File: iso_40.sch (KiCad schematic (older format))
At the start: 14 parts

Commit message: layout png
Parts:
- added F?: 500mA, symbol Device:Polyfuse_Small
- added USB?: Molex-0548190589, symbol random-keyboard-parts:Molex-0548190589
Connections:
- net +5V: now also F?.1
- net D+: now also USB?.3 (D+)
- net D-: now also USB?.4 (D-)
- net GND: now also USB?.1 (GND)
- new net VCC: F?.2, USB?.5 (VBUS)
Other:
- moved on the sheet: C?, R?, SW?, U?, Y?

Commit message: pcb routed
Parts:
- added D1, D10, D11, D12, D13, D14, D15, D16, D17, D18, D19, D2, D20, D21, D22, D23, D24, D25, D26, D27, D28, D29, D3, D30, D31, D32, D33, D34, D35, D36, D37, D38, D39, D4, D40, D5, D6, D7, D8, D9: SOD-123, Diode_SMD:D_SOD-123, symbol Device:D_Small
- added MX1, MX10, MX11, MX14, MX15, MX16, MX17, MX18, MX19, MX2, MX20, MX21, MX22, MX23, MX25, MX26, MX27, MX28, MX29, MX3, MX30, MX31, MX32, MX33, MX34, MX35, MX36, MX4, MX40, MX5, MX6, MX7, MX8, MX9: MX-NoLED, MX_Only:MXOnly-1U-NoLED, symbol MX_Alps_Hybrid:MX-NoLED
- added MX12: MX-NoLED, MX_Only:MXOnly-ISO, symbol MX_Alps_Hybrid:MX-NoLED
- added MX13: MX-NoLED, MX_Only:MXOnly-1.25U-NoLED, symbol MX_Alps_Hybrid:MX-NoLED
- added MX24, MX37, MX39: MX-NoLED, MX_Only:MXOnly-1.5U-NoLED, symbol MX_Alps_Hybrid:MX-NoLED
- added MX38: MX-NoLED, MX_Only:MXOnly-6U-NoLED, symbol MX_Alps_Hybrid:MX-NoLED
- C1, C2, C3, C4, C5, C6, C7: renamed from C?; footprint (none) -> Capacitor_SMD:C_0805_2012Metric
- F1: renamed from F?; footprint (none) -> Fuse:Fuse_1206_3216Metric
- R1, R2, R3, R4: renamed from R?; footprint (none) -> Resistor_SMD:R_0805_2012Metric
- SW1: renamed from SW?; footprint (none) -> random-keyboard-parts:SKQG-1155865
- USB1: renamed from USB?; footprint (none) -> random-keyboard-parts:Molex-0548190589
- Y1: renamed from Y?; footprint (none) -> Crystal:Crystal_SMD_3225-4Pin_3.2x2.5mm
- gave numbers to parts that had none: 1
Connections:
- net col_08: now reaches U1.10 (PB2)
- net col_08: now also MX21.1 (COL), MX32.1 (COL), MX9.1 (COL)
- net col_09: now reaches U1.11 (PB3)
- net col_09: now also MX10.1 (COL), MX22.1 (COL), MX33.1 (COL), MX39.1 (COL)
- net col_06: now reaches U1.12 (PB7)
- net col_06: now also MX19.1 (COL), MX30.1 (COL), MX38.1 (COL), MX7.1 (COL)
- net col_10: now reaches U1.18 (PD0)
- net col_10: now also MX11.1 (COL), MX23.1 (COL), MX34.1 (COL), MX40.1 (COL)
- net col_11: now reaches U1.19 (PD1)
- net col_11: now also MX12.1 (COL), MX35.1 (COL)
- net row_2: now reaches U1.20 (PD2)
- net row_2: now also D24.1 (K), D25.1 (K), D26.1 (K), D27.1 (K), D28.1 (K), D29.1 (K), D30.1 (K), D31.1 (K), D32.1 (K), D33.1 (K), D34.1 (K), D35.1 (K)
- net row_1: now reaches U1.21 (PD3)
- net row_1: now also D13.1 (K), D14.1 (K), D15.1 (K), D16.1 (K), D17.1 (K), D18.1 (K), D19.1 (K), D20.1 (K), D21.1 (K), D22.1 (K), D23.1 (K)
- net row_0: now reaches U1.22 (PD5)
- net row_0: now also D1.1 (K), D10.1 (K), D11.1 (K), D12.1 (K), D2.1 (K), D3.1 (K), D4.1 (K), D5.1 (K), D6.1 (K), D7.1 (K), D8.1 (K), D9.1 (K)
- net row_3: now reaches U1.25 (PD4)
- net row_3: now also D36.1 (K), D37.1 (K), D38.1 (K), D39.1 (K), D40.1 (K)
- net col_04: now reaches U1.37 (PF6)
- net col_04: now also MX17.1 (COL), MX28.1 (COL), MX5.1 (COL)
- net col_03: now reaches U1.38 (PF5)
- net col_03: now also MX16.1 (COL), MX27.1 (COL), MX4.1 (COL)
- net col_02: now reaches U1.39 (PF4)
- net col_02: now also MX15.1 (COL), MX26.1 (COL), MX3.1 (COL)
- net col_01: now reaches U1.40 (PF1)
- net col_01: now also MX14.1 (COL), MX2.1 (COL), MX25.1 (COL), MX37.1 (COL)
- net col_00: now reaches U1.41 (PF0)
- net col_00: now also MX1.1 (COL), MX13.1 (COL), MX24.1 (COL), MX36.1 (COL)
- net col_05: now reaches U1.8 (PB0)
- net col_05: now also MX18.1 (COL), MX29.1 (COL), MX6.1 (COL)
- net col_07: now reaches U1.9 (PB1)
- net col_07: now also MX20.1 (COL), MX31.1 (COL), MX8.1 (COL)
- new net: D1.2 (A), MX1.2 (ROW)
- new net: D2.2 (A), MX2.2 (ROW)
- new net: D3.2 (A), MX3.2 (ROW)
- new net: D4.2 (A), MX4.2 (ROW)
- new net: D5.2 (A), MX5.2 (ROW)
- new net: D6.2 (A), MX6.2 (ROW)
- new net: D7.2 (A), MX7.2 (ROW)
- new net: D8.2 (A), MX8.2 (ROW)
- new net: D9.2 (A), MX9.2 (ROW)
- new net: D10.2 (A), MX10.2 (ROW)
- new net: D11.2 (A), MX11.2 (ROW)
- new net: D12.2 (A), MX12.2 (ROW)
- new net: D13.2 (A), MX13.2 (ROW)
- new net: D14.2 (A), MX14.2 (ROW)
- new net: D15.2 (A), MX15.2 (ROW)
- new net: D16.2 (A), MX16.2 (ROW)
- new net: D17.2 (A), MX17.2 (ROW)
- new net: D18.2 (A), MX18.2 (ROW)
- new net: D19.2 (A), MX19.2 (ROW)
- new net: D20.2 (A), MX20.2 (ROW)
- new net: D21.2 (A), MX21.2 (ROW)
- new net: D22.2 (A), MX22.2 (ROW)
- new net: D23.2 (A), MX23.2 (ROW)
- new net: D24.2 (A), MX24.2 (ROW)
- new net: D25.2 (A), MX25.2 (ROW)
- new net: D26.2 (A), MX26.2 (ROW)
- new net: D27.2 (A), MX27.2 (ROW)
- new net: D28.2 (A), MX28.2 (ROW)
- new net: D29.2 (A), MX29.2 (ROW)
- new net: D30.2 (A), MX30.2 (ROW)
- new net: D31.2 (A), MX31.2 (ROW)
- new net: D32.2 (A), MX32.2 (ROW)
- new net: D33.2 (A), MX33.2 (ROW)
- new net: D34.2 (A), MX34.2 (ROW)
- new net: D35.2 (A), MX35.2 (ROW)
- new net: D37.2 (A), MX37.2 (ROW)
- new net: D36.2 (A), MX36.2 (ROW)
- new net: D38.2 (A), MX38.2 (ROW)
- new net: D40.2 (A), MX40.2 (ROW)
- new net: D39.2 (A), MX39.2 (ROW)
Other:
- moved on the sheet: F1, USB1

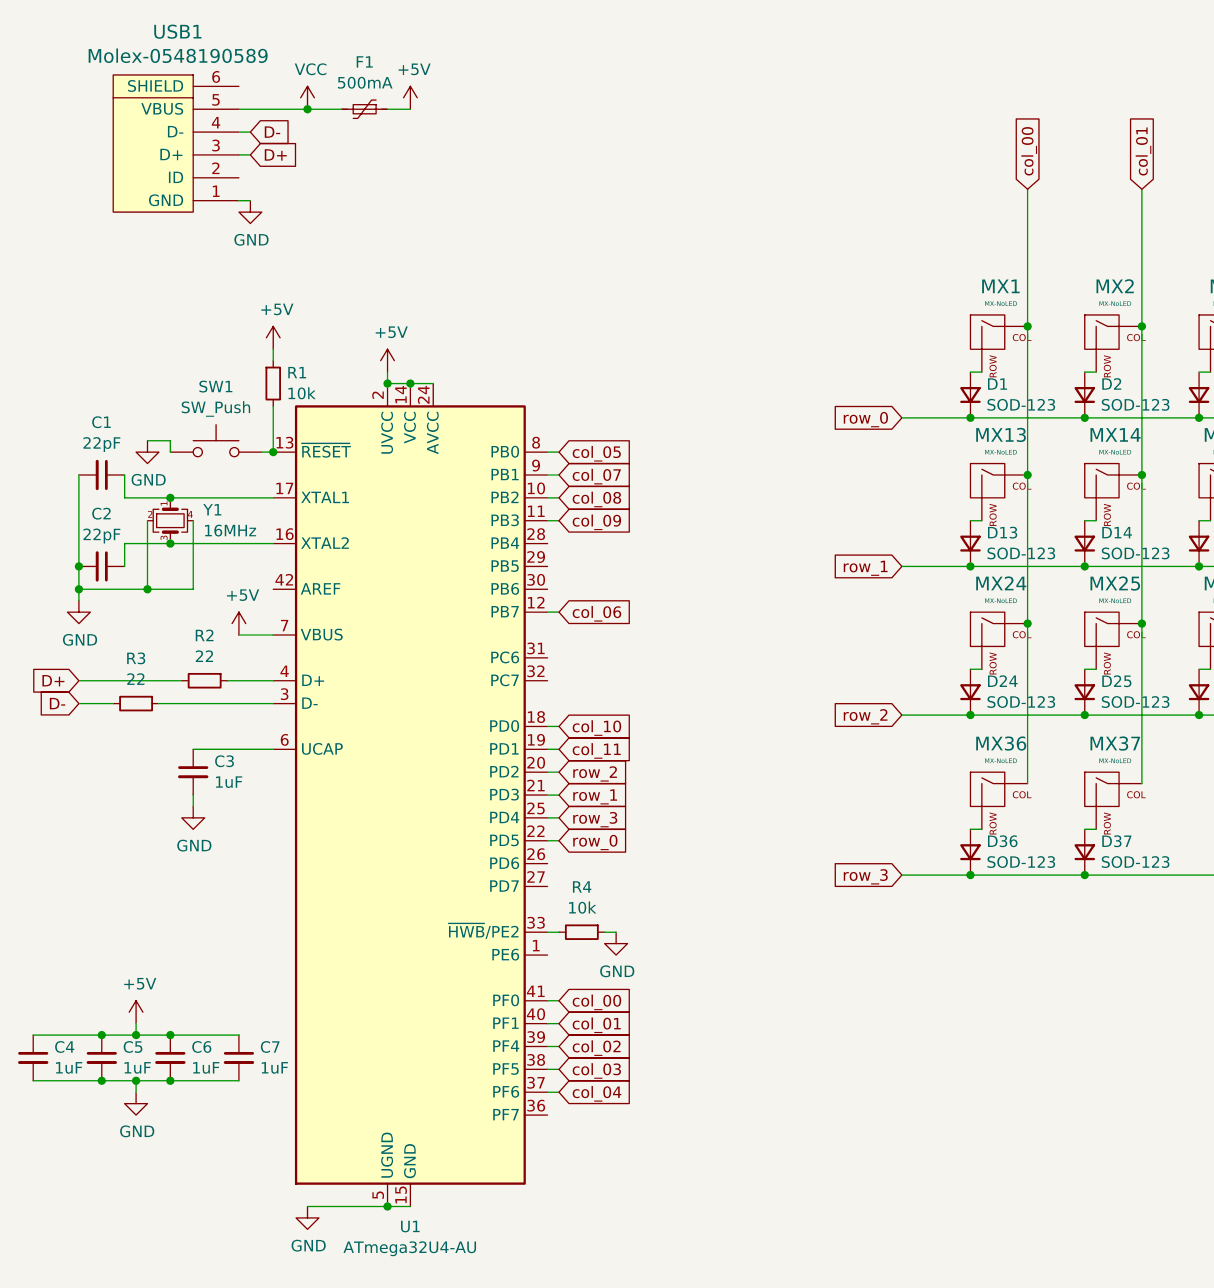
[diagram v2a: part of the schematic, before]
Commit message: ISP header added
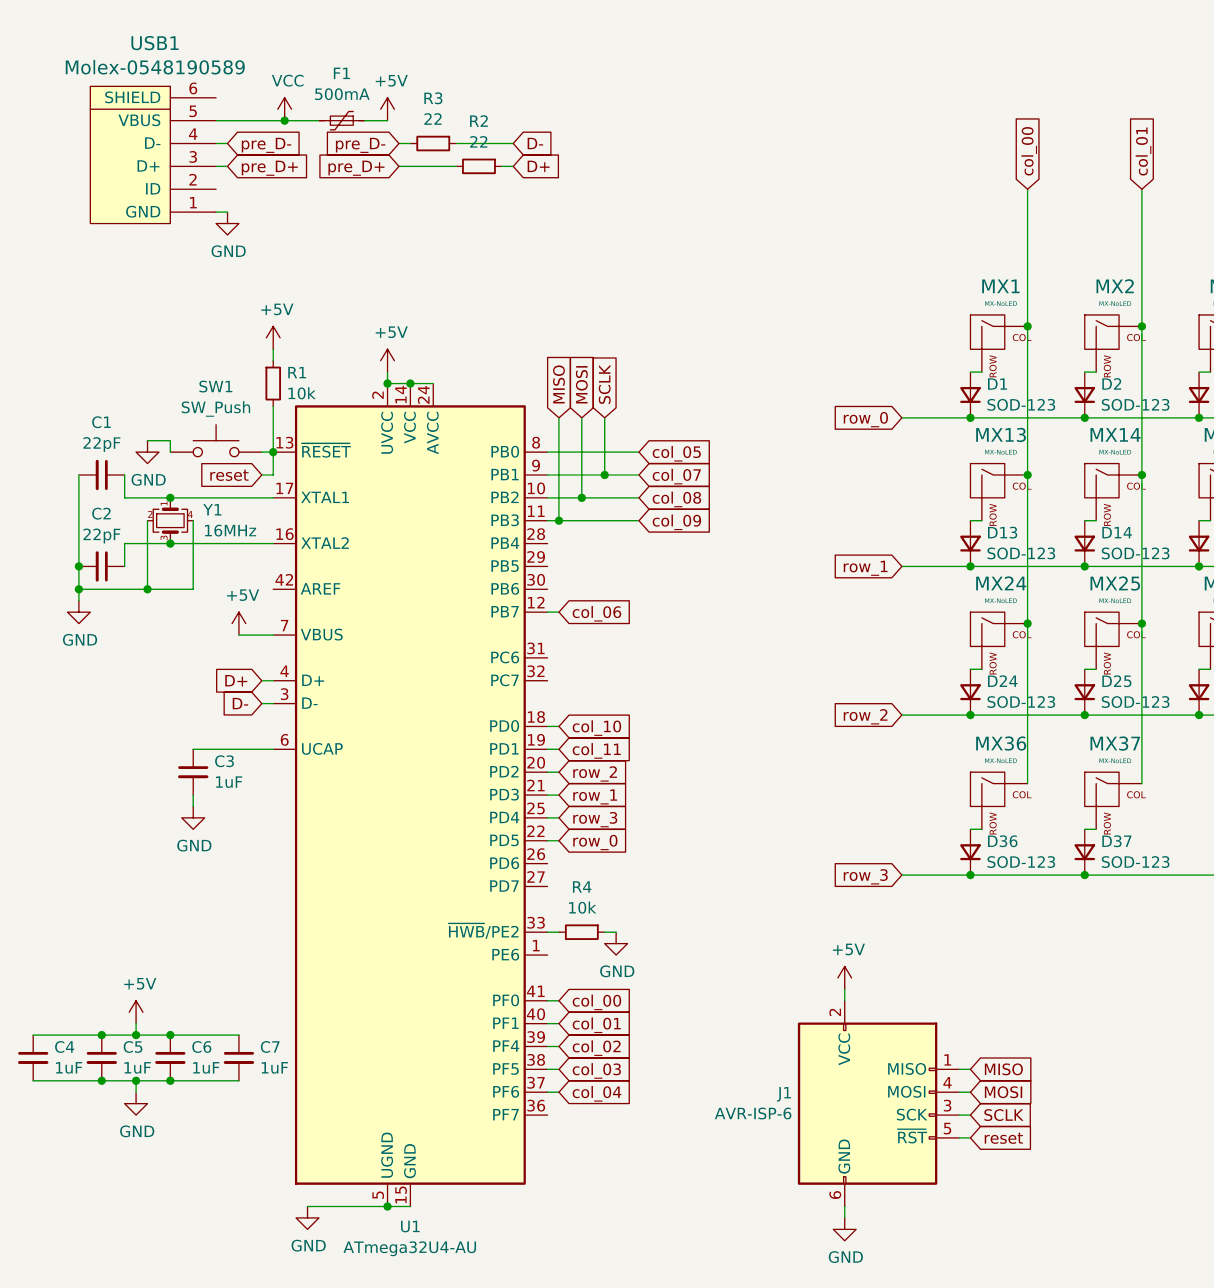
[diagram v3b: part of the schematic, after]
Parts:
- added J1: AVR-ISP-6, Connector_PinHeader_2.54mm:PinHeader_2x03_P2.54mm_Vertical, symbol Connector:AVR-ISP-6
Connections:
- net +5V: now also J1.2 (VCC)
- net D+: now also R2.1, U1.4 (D+); no longer R2.2, USB1.3 (D+)
- net D-: now also R3.1, U1.3 (D-); no longer R3.2, USB1.4 (D-)
- net GND: now also J1.6 (GND)
- net reset: now reaches R1.2, SW1.2, U1.13 (~RESET)
- net reset: now also J1.5 (~RST)
- net col_07 renamed SCLK
- net SCLK: now also J1.3 (SCK)
- net col_08 renamed MOSI
- net MOSI: now also J1.4 (MOSI)
- net col_09 renamed MISO
- net MISO: now also J1.1 (MISO)
- new net pre_D+: R2.2, USB1.3 (D+)
- new net pre_D-: R3.2, USB1.4 (D-)
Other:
- moved on the sheet: F1, R2, R3, USB1
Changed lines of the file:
@@
 L Device:R_Small R3
 U 1 1 5F1598E0
-P 1100 5250
-F 0 "R3" V 904 5250 50  0000 C CNN
-F 1 "22" V 995 5250 50  0000 C CNN
-F 2 "Resistor_SMD:R_0805_2012Metric" H 1100 5250 50  0001 C CNN
-F 3 "~" H 1100 5250 50  0001 C CNN
-	1    1100 5250
+P 2400 2800
+F 0 "R3" V 2204 2800 50  0000 C CNN
+F 1 "22" V 2295 2800 50  0000 C CNN
+F 2 "Resistor_SMD:R_0805_2012Metric" H 2400 2800 50  0001 C CNN
+F 3 "~" H 2400 2800 50  0001 C CNN
+	1    2400 2800
 	0    1    1    0
 $EndComp
@@
 L Device:R_Small R2
 U 1 1 5F1590A4
-P 1400 5150
-F 0 "R2" V 1204 5150 50  0000 C CNN
-F 1 "22" V 1295 5150 50  0000 C CNN
-F 2 "Resistor_SMD:R_0805_2012Metric" H 1400 5150 50  0001 C CNN
-F 3 "~" H 1400 5150 50  0001 C CNN
-	1    1400 5150
+P 2600 2900
+F 0 "R2" V 2404 2900 50  0000 C CNN
+F 1 "22" V 2495 2900 50  0000 C CNN
+F 2 "Resistor_SMD:R_0805_2012Metric" H 2600 2900 50  0001 C CNN
+F 3 "~" H 2600 2900 50  0001 C CNN
+	1    2600 2900
 	0    1    1    0
 $EndComp
-Wire Wire Line
-	1700 5150 1500 5150
-Wire Wire Line
-	1700 5250 1200 5250
 $Comp
 L Device:Crystal_GND24_Small Y1
@@
 Wire Wire Line
 	1700 3700 1700 3750
-Text GLabel 850  5150 0    50   Input ~ 0
+Text GLabel 1650 5150 0    50   Input ~ 0
 D+
-Text GLabel 850  5250 0    50   Input ~ 0
+Text GLabel 1650 5250 0    50   Input ~ 0
 D-
-Wire Wire Line
-	850  5150 1300 5150
-Wire Wire Line
-	850  5250 1000 5250
 $Comp
 L random-keyboard-parts:Molex-0548190589 USB1
 U 1 1 5F1AE520
-P 1250 2850
-F 0 "USB1" V 1787 2817 60  0000 C CNN
-F 1 "Molex-0548190589" V 1681 2817 60  0000 C CNN
-F 2 "random-keyboard-parts:Molex-0548190589" H 1250 2850 60  0001 C CNN
-F 3 "" H 1250 2850 60  0001 C CNN
-	1    1250 2850
+P 1150 2900
+F 0 "USB1" V 1687 2867 60  0000 C CNN
+F 1 "Molex-0548190589" V 1581 2867 60  0000 C CNN
+F 2 "random-keyboard-parts:Molex-0548190589" H 1150 2900 60  0001 C CNN
+F 3 "" H 1150 2900 60  0001 C CNN
+	1    1150 2900
 	0    -1   -1   0
 $EndComp
@@
 L Device:Polyfuse_Small F1
 U 1 1 5F1B31E3
-P 2100 2650
-F 0 "F1" V 1895 2650 50  0000 C CNN
-F 1 "500mA" V 1986 2650 50  0000 C CNN
-F 2 "Fuse:Fuse_1206_3216Metric" H 2150 2450 50  0001 L CNN
-F 3 "~" H 2100 2650 50  0001 C CNN
-	1    2100 2650
+P 2000 2700
+F 0 "F1" V 1795 2700 50  0000 C CNN
+F 1 "500mA" V 1886 2700 50  0000 C CNN
+F 2 "Fuse:Fuse_1206_3216Metric" H 2050 2500 50  0001 L CNN
+F 3 "~" H 2000 2700 50  0001 C CNN
+	1    2000 2700
 	0    1    1    0
 $EndComp
@@
 L power:+5V #PWR0111
 U 1 1 5F1B4443
-P 2300 2650
-F 0 "#PWR0111" H 2300 2500 50  0001 C CNN
-F 1 "+5V" H 2315 2823 50  0000 C CNN
-F 2 "" H 2300 2650 50  0001 C CNN
-F 3 "" H 2300 2650 50  0001 C CNN
-	1    2300 2650
-	1    0    0    -1
-$EndComp
-Wire Wire Line
-	2300 2650 2200 2650
+P 2200 2700
+F 0 "#PWR0111" H 2200 2550 50  0001 C CNN
+F 1 "+5V" H 2215 2873 50  0000 C CNN
+F 2 "" H 2200 2700 50  0001 C CNN
+F 3 "" H 2200 2700 50  0001 C CNN
+	1    2200 2700
+	1    0    0    -1
+$EndComp
+Wire Wire Line
+	2200 2700 2100 2700
 $Comp
 L power:VCC #PWR0112
 U 1 1 5F1B5D09
-P 1850 2650
-F 0 "#PWR0112" H 1850 2500 50  0001 C CNN
-F 1 "VCC" H 1865 2823 50  0000 C CNN
-F 2 "" H 1850 2650 50  0001 C CNN
-F 3 "" H 1850 2650 50  0001 C CNN
-	1    1850 2650
-	1    0    0    -1
-$EndComp
-Wire Wire Line
-	1550 2650 1850 2650
-Wire Wire Line
-	1850 2650 2000 2650
-Connection ~ 1850 2650
-Text GLabel 1600 2750 2    50   Input ~ 0
+P 1750 2700
+F 0 "#PWR0112" H 1750 2550 50  0001 C CNN
+F 1 "VCC" H 1765 2873 50  0000 C CNN
+F 2 "" H 1750 2700 50  0001 C CNN
+F 3 "" H 1750 2700 50  0001 C CNN
+	1    1750 2700
+	1    0    0    -1
+$EndComp
+Wire Wire Line
+	1450 2700 1750 2700
+Wire Wire Line
+	1750 2700 1900 2700
+Connection ~ 1750 2700
+Text GLabel 2750 2800 2    50   Input ~ 0
 D-
-Text GLabel 1600 2850 2    50   Input ~ 0
+Text GLabel 2750 2900 2    50   Input ~ 0
 D+
-Wire Wire Line
-	1550 2750 1600 2750
-Wire Wire Line
-	1550 2850 1600 2850
 $Comp
 L power:GND #PWR0113
 U 1 1 5F1BDF98
-P 1600 3050
-F 0 "#PWR0113" H 1600 2800 50  0001 C CNN
-F 1 "GND" H 1605 2877 50  0000 C CNN
-F 2 "" H 1600 3050 50  0001 C CNN
-F 3 "" H 1600 3050 50  0001 C CNN
-	1    1600 3050
-	1    0    0    -1
-$EndComp
-Wire Wire Line
-	1550 3050 1600 3050
+P 1500 3100
+F 0 "#PWR0113" H 1500 2850 50  0001 C CNN
+F 1 "GND" H 1505 2927 50  0000 C CNN
+F 2 "" H 1500 3100 50  0001 C CNN
+F 3 "" H 1500 3100 50  0001 C CNN
+	1    1500 3100
+	1    0    0    -1
+$EndComp
+Wire Wire Line
+	1450 3100 1500 3100
 $Comp
 L MX_Alps_Hybrid:MX-NoLED MX1
@@
 Text GLabel 2950 6950 2    50   Input ~ 0
 col_04
-Text GLabel 2950 4150 2    50   Input ~ 0
+Text GLabel 3300 4150 2    50   Input ~ 0
 col_05
 Wire Wire Line
@@
 Text GLabel 2950 4850 2    50   Input ~ 0
 col_06
-Text GLabel 2950 4250 2    50   Input ~ 0
+Text GLabel 3300 4250 2    50   Input ~ 0
 col_07
-Text GLabel 2950 4350 2    50   Input ~ 0
+Text GLabel 3300 4350 2    50   Input ~ 0
 col_08
 Wire Wire Line
-	2950 4150 2900 4150
-Wire Wire Line
 	2950 4850 2900 4850
-Wire Wire Line
-	2950 4250 2900 4250
-Wire Wire Line
-	2950 4350 2900 4350
-Text GLabel 2950 4450 2    50   Input ~ 0
+Text GLabel 3300 4450 2    50   Input ~ 0
 col_09
-Wire Wire Line
-	2950 4450 2900 4450
 Text GLabel 2950 5350 2    50   Input ~ 0
 col_10
@@
 Wire Wire Line
 	2950 5850 2900 5850
+$Comp
+L Connector:AVR-ISP-6 J1
+U 1 1 5F1E7AF3
+P 4300 7050
+F 0 "J1" H 3971 7146 50  0000 R CNN
+F 1 "AVR-ISP-6" H 3971 7055 50  0000 R CNN
+F 2 "Connector_PinHeader_2.54mm:PinHeader_2x03_P2.54mm_Vertical" V 4050 7100 50  0001 C CNN
+F 3 " ~" H 3025 6500 50  0001 C CNN
+	1    4300 7050
+	1    0    0    -1
+$EndComp
+$Comp
+L power:GND #PWR0114
+U 1 1 5F217378
+P 4200 7500
+F 0 "#PWR0114" H 4200 7250 50  0001 C CNN
+F 1 "GND" H 4205 7327 50  0000 C CNN
+F 2 "" H 4200 7500 50  0001 C CNN
+F 3 "" H 4200 7500 50  0001 C CNN
+	1    4200 7500
+	1    0    0    -1
+$EndComp
+Wire Wire Line
+	4200 7450 4200 7500
+Text GLabel 4750 7150 2    50   Input ~ 0
+reset
+Text GLabel 4750 7050 2    50   Input ~ 0
+SCLK
+Text GLabel 4750 6950 2    50   Input ~ 0
+MOSI
+Text GLabel 4750 6850 2    50   Input ~ 0
+MISO
+Wire Wire Line
+	4700 6850 4750 6850
+Wire Wire Line
+	4700 6950 4750 6950
+Wire Wire Line
+	4700 7050 4750 7050
+Wire Wire Line
+	4700 7150 4750 7150
+$Comp
+L power:+5V #PWR0115
+U 1 1 5F250041
+P 4200 6500
+F 0 "#PWR0115" H 4200 6350 50  0001 C CNN
+F 1 "+5V" H 4215 6673 50  0000 C CNN
+F 2 "" H 4200 6500 50  0001 C CNN
+F 3 "" H 4200 6500 50  0001 C CNN
+	1    4200 6500
+	1    0    0    -1
+$EndComp
+Wire Wire Line
+	4200 6500 4200 6550
+Text GLabel 1650 4250 0    50   Input ~ 0
+reset
+Wire Wire Line
+	1650 4250 1700 4250
+Wire Wire Line
+	1700 4250 1700 4150
+Wire Wire Line
+	2900 4350 3050 4350
+Wire Wire Line
+	2900 4250 3150 4250
+Text GLabel 2950 4000 1    50   Input ~ 0
+MISO
+Text GLabel 3050 4000 1    50   Input ~ 0
+MOSI
+Text GLabel 3150 4000 1    50   Input ~ 0
+SCLK
+Wire Wire Line
+	3150 4000 3150 4250
+Connection ~ 3150 4250
+Wire Wire Line
+	3150 4250 3300 4250
+Wire Wire Line
+	3050 4000 3050 4350
+Connection ~ 3050 4350
+Wire Wire Line
+	3050 4350 3300 4350
+Wire Wire Line
+	2900 4450 2950 4450
+Wire Wire Line
+	2900 4150 3300 4150
+Wire Wire Line
+	2950 4000 2950 4450
+Connection ~ 2950 4450
+Wire Wire Line
+	2950 4450 3300 4450
+Wire Wire Line
+	1700 5150 1650 5150
+Wire Wire Line
+	1700 5250 1650 5250
+Wire Wire Line
+	2750 2900 2700 2900
+Wire Wire Line
+	2750 2800 2500 2800
+Text GLabel 1500 2800 2    50   Input ~ 0
+pre_D-
+Text GLabel 1500 2900 2    50   Input ~ 0
+pre_D+
+Wire Wire Line
+	1450 2800 1500 2800
+Wire Wire Line
+	1450 2900 1500 2900
+Text GLabel 2250 2800 0    50   Input ~ 0
+pre_D-
+Text GLabel 2250 2900 0    50   Input ~ 0
+pre_D+
+Wire Wire Line
+	2250 2800 2300 2800
+Wire Wire Line
+	2250 2900 2500 2900
 $EndSCHEMATC
